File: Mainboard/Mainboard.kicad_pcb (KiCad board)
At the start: 2 copper layers, 60 x 95 mm, 28 parts, among them J1 Bus_M.2_Socket_E, J3 USB_A_Stacked, J4 Micro_SD_Card, J6 Conn_01x09_Pin, J7 Conn_01x09_Pin, U1 Hirose DF40C-100DS-0.4V, U2 ADS1115IDGS, U3 PCM5102, U4 PAM8403D

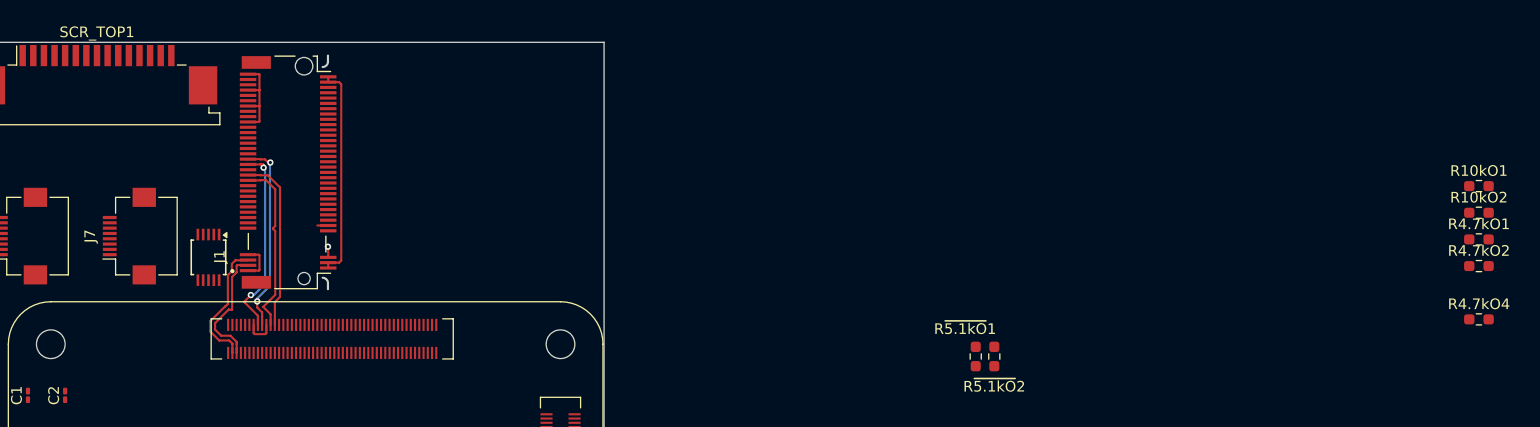
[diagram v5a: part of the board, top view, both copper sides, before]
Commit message: Wifi Card Connected!
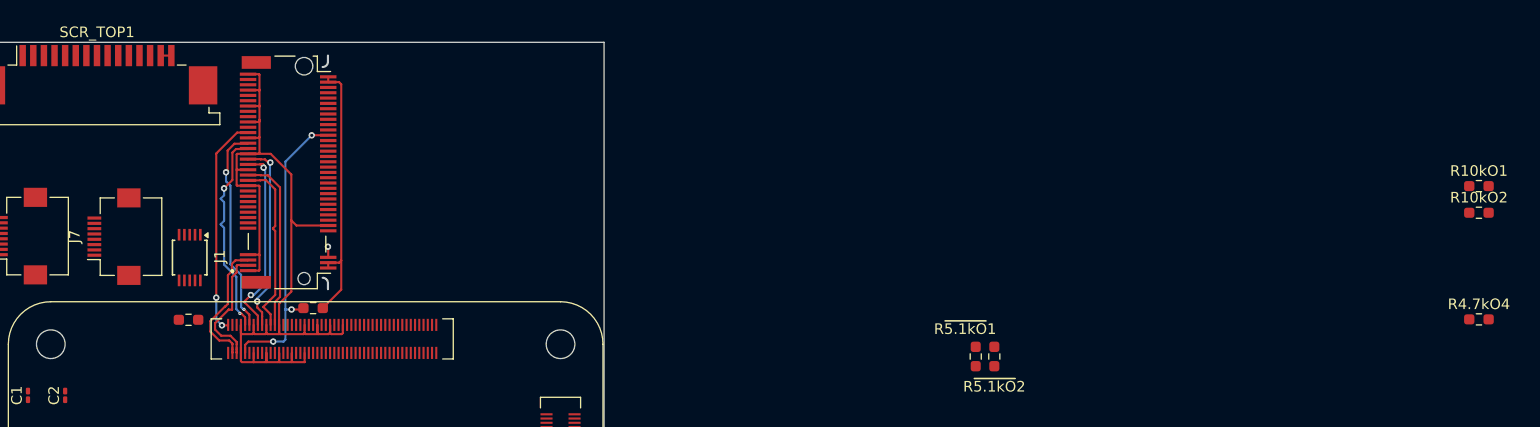
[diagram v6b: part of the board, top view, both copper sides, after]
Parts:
- moved R4.7kO1 121.8 mm to (115.9, 78.6), turned to 180 degrees
- moved R4.7kO2 109.9 mm to (127.6, 77.5)
- moved U2 1.77 mm to (116.0, 72.8)
- moved J7 1.45 mm to (108.8, 70.8)
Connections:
- net Net-(J1-REFCLKn0) renamed /RFCLK-
- net Net-(J1-REFCLKp0) renamed /RFCLK+
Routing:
- net GND: track 16.2 -> 89.5 mm
- net Net-(J1-~{PERST0}): track 0.00 -> 28.3 mm, vias 0 -> 3
- net Net-(J1-~{CLKREQ0}): track 0.00 -> 20.8 mm, vias 0 -> 2
- net /RFCLK+: track 0.00 -> 19.7 mm, vias 0 -> 2
- net /RFCLK-: track 0.00 -> 19.6 mm, vias 0 -> 2
- net /3V3: track 20.3 -> 26.5 mm
